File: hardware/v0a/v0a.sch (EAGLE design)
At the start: 117 parts, among them J1 2EDG-2P, J2 2EDG-2P, J3 2EDG-2P, J4 2EDG-2P, Q1 IRF7580, Q2 IRF7580, Q3 IRF7580, Q4 IRF7580, Q5 IRF7580, Q6 IRF7580, Q7 IRF7580, Q8 IRF7580, U1 TMC4671, U10 AD8418, U11 AD8418, U2 MIC39101, U3 MIC39101, U4 SI82397, U5 SI82397, U6 SI82397, U7 SI82397, U8 MIC4682, U9 CP2130

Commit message: temp
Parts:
- added C31: (no value), Passive Components > Capacitors > Multilayer Ceramic Capacitors MLCC:MLCC0603
- added C69, C70: 100p, Passive Components > Capacitors > Multilayer Ceramic Capacitors MLCC:MLCC0603
- added C71: 10n, Passive Components > Capacitors > Multilayer Ceramic Capacitors MLCC:MLCC0603
- added D8: BAT54S, Semiconductors > Discrete Semiconductors > Diodes & Rectifiers > Schottky Diodes & Rectifiers:BAT54S
- added R15, R16, R17, R18, R19, R20, R21, R22, R23, R24, R26, R32, R33, R34, R35: 10k, Passive Components > Resistors > Chip Resistors:RESISTOR0603
- added R25, R27: (no value), Passive Components > Resistors > Chip Resistors:RESISTOR0603
- added R28, R29, R30, R31: 2.2, Passive Components > Resistors > Chip Resistors:RESISTOR0603
- added R36, R37: 100, Passive Components > Resistors > Chip Resistors:RESISTOR0603
- added R38: 100k, Passive Components > Resistors > Chip Resistors:RESISTOR0603
- added R39: 1k5, Passive Components > Resistors > Chip Resistors:RESISTOR0603
- added U12: DSC1101, Eletromechanical > MEMS Oscillators:DSC1101
- R1, R2, R3, R4, R5, R6, R7, R8: value (none) -> 2.2
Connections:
- new net N$38: R15.P$2, U1-SENSO.PWM_IDLE_L@60
- new net N$39: R16.P$2, U1-SENSO.PWM_IDLE_H@59
- new net N$40: D4.A, R31.P$2
- new net N$41: U1-MISC.CLK@51, U12.OUT@4
- new net N$42: R27.P$2, U1-MISC.!RST!@50
- new net N$43: D3.A, R30.P$2
- new net N$44: R25.P$1, U12.EN@1
- new net N$48: D2.A, R29.P$2
- new net N$49: D1.A, R28.P$2
- new net N$50: C69.P$1, R36.P$1, U1-SENSO.ADC_I0_POS@16
- new net N$51: C70.P$1, R37.P$1, U1-SENSO.ADC_I1_POS@18
- new net N$52: R32.P$1, R33.P$2, U1-SENSO.ADC_I0_NEG@17
- new net N$53: R34.P$1, R35.P$2, U1-SENSO.ADC_I1_NEG@19
- new net N$54: C71.P$1, D8.3, R38.P$1, R39.P$2, U1-SENSO.ADC_VM@20
- net !CS: now also U1-IO.SPI_NSCS@6
- net 12V: now also R28.P$1, R29.P$1, R30.P$1, R31.P$1; no longer D1.A, D2.A, D3.A, D4.A
- net 3.3V: now also C31.P$1, R25.P$2, R27.P$1, U12.VDD@6
- net 5V: now also D8.1, R32.P$2, R34.P$2
- net ADC_I0_U_PF: now also R36.P$2
- net ADC_I1_V_PF: now also R37.P$2
- net DCBUS: now also R38.P$2
- net ENO: now also R26.P$1, U1-IO.ENO@32
- net GND: now also C31.P$2, C69.P$2, C70.P$2, C71.P$2, D8.2, R15.P$1, R16.P$1, R17.P$1, R18.P$1, R19.P$1, R20.P$1, R21.P$1, R22.P$1, R23.P$1, R24.P$1, R26.P$2, R33.P$1, R35.P$1, R39.P$1, U$10.GND@1, U1-MISC.TEST@54, U12.GND@3; no longer U$10.CASE
- net INT: now also U1-MISC.STATUS@12
- net MISO: now also U1-IO.SPI_MISO@9
- net MOSI: now also U1-IO.SPI_MOSI@8
- net N$11: no longer D2.C
- net N$30: now also U$10.D+; no longer U$10.VBUS
- net N$31: now also U$10.D-; no longer U$10.D+
- net N$32: now also U$10.VBUS; no longer U$10.D-
- net PWM_UX1_H: now also R17.P$2, U1-SENSO.PWM_UX1_H@39
- net PWM_UX1_L: now also R18.P$2, U1-SENSO.PWM_UX1_L@40
- net PWM_VX2_H: now also R19.P$2, U1-SENSO.PWM_VX2_H@41
- net PWM_VX2_L: now also R20.P$2, U1-SENSO.PWM_VX2_L@42
- net PWM_WY1_H: now also R21.P$2, U1-SENSO.PWM_WY1_H@46
- net PWM_WY1_L: now also R22.P$2, U1-SENSO.PWM_WY1_L@47
- net PWM_Y2_H: now also R23.P$2, U1-SENSO.PWM_Y2_H@48
- net PWM_Y2_L: now also R24.P$2, U1-SENSO.PWM_Y2_L@49
- net SCK: now also U1-IO.SPI_SCK@7
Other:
- moved on the sheet: D1, D2, D3, D4, U1-MISC

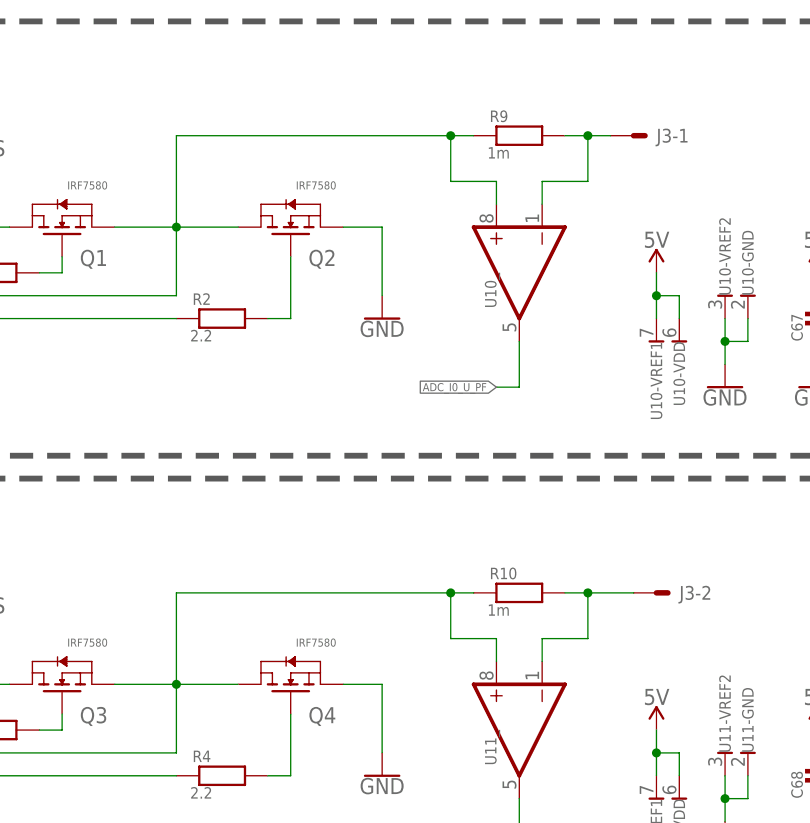
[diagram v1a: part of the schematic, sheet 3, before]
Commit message: changed current sense resistors to 700u
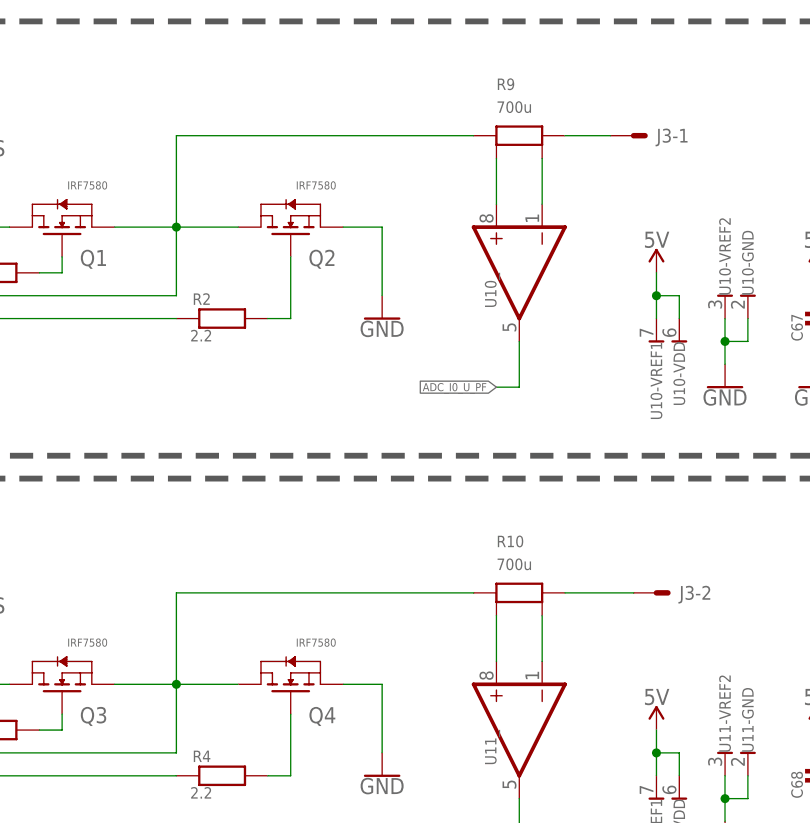
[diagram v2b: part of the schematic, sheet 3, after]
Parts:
- R10, R9: value 1m -> 700u; device Passive Components > Resistors > Current Sense:WSLF25121L000FEA -> Passive Components > Resistors > Current Sense:LRMAP3920
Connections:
- new net N$55: R10.SENSE-, U11_.IN-@1
- new net N$56: R10.SENSE+, U11_.IN+@8
- new net N$57: R9.SENSE-, U10_.IN-@1
- new net N$58: R9.SENSE+, U10_.IN+@8
- net N$10: no longer U11_.IN+@8
- net N$28: no longer U11_.IN-@1
- net N$29: no longer U10_.IN-@1
- net N$6: no longer U10_.IN+@8
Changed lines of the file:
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@@
 <part name="R8" library="Passive Components &gt; Resistors &gt; Chip Resistors" deviceset="RESISTOR" device="0603" value="2.2"/>
 <part name="J4" library="Connectors &gt; Other" deviceset="2EDG-2P" device=""/>
-<part name="R9" library="Passive Components &gt; Resistors &gt; Current Sense" deviceset="WSLF25121L000FEA" device="" value="1m"/>
 <part name="U10" library="Semiconductors &gt; Integrated Circuits - ICs &gt; Amplifier ICs &gt; Current Sense Amplifiers" deviceset="AD8418" device=""/>
 <part name="GND36" library="Utility &gt; Power Symbols" deviceset="GND" device=""/>
@@
 <part name="GND38" library="Utility &gt; Power Symbols" deviceset="GND" device=""/>
 <part name="C67" library="Passive Components &gt; Capacitors &gt; Multilayer Ceramic Capacitors MLCC" deviceset="MLCC" device="0603"/>
-<part name="R10" library="Passive Components &gt; Resistors &gt; Current Sense" deviceset="WSLF25121L000FEA" device="" value="1m"/>
 <part name="U11" library="Semiconductors &gt; Integrated Circuits - ICs &gt; Amplifier ICs &gt; Current Sense Amplifiers" deviceset="AD8418" device=""/>
 <part name="GND40" library="Utility &gt; Power Symbols" deviceset="GND" device=""/>
@@
 <part name="GND73" library="Utility &gt; Power Symbols" deviceset="GND" device=""/>
 <part name="GND74" library="Utility &gt; Power Symbols" deviceset="GND" device=""/>
+<part name="R9" library="Passive Components &gt; Resistors &gt; Current Sense" deviceset="LRMAP3920" device="" value="700u"/>
+<part name="R10" library="Passive Components &gt; Resistors &gt; Current Sense" deviceset="LRMAP3920" device="" value="700u"/>
 </parts>
 <sheets>
@@
 <attribute name="NAME" x="233.68" y="75.438" size="1.524" layer="95"/>
 </instance>
-<instance part="R9" gate="G$1" x="256.54" y="228.6" smashed="yes">
-<attribute name="NAME" x="253.238" y="230.124" size="1.27" layer="95"/>
-<attribute name="VALUE" x="252.984" y="226.06" size="1.27" layer="96"/>
-</instance>
 <instance part="U10" gate="_" x="256.54" y="208.28" smashed="yes" rot="MR270">
 <attribute name="NAME" x="254" y="213.36" size="1.27" layer="95" ratio="15" rot="MR270"/>
@@
 <attribute name="VALUE" x="292.1" y="205.74" size="1.27" layer="96" rot="R90"/>
 </instance>
-<instance part="R10" gate="G$1" x="256.54" y="177.8" smashed="yes">
-<attribute name="NAME" x="253.238" y="179.324" size="1.27" layer="95"/>
-<attribute name="VALUE" x="252.984" y="175.26" size="1.27" layer="96"/>
-</instance>
 <instance part="U11" gate="_" x="256.54" y="157.48" smashed="yes" rot="MR270">
 <attribute name="NAME" x="254" y="162.56" size="1.27" layer="95" ratio="15" rot="MR270"/>
@@
 <attribute name="NAME" x="144.018" y="82.804" size="1.27" layer="95"/>
 <attribute name="VALUE" x="143.764" y="78.74" size="1.27" layer="96"/>
+</instance>
+<instance part="R9" gate="G$1" x="256.54" y="228.6" smashed="yes">
+<attribute name="NAME" x="254" y="233.68" size="1.27" layer="95"/>
+<attribute name="VALUE" x="254" y="231.14" size="1.27" layer="96"/>
+</instance>
+<instance part="R10" gate="G$1" x="256.54" y="177.8" smashed="yes">
+<attribute name="NAME" x="254" y="182.88" size="1.27" layer="95"/>
+<attribute name="VALUE" x="254" y="180.34" size="1.27" layer="96"/>
 </instance>
 </instances>
@@
 <pinref part="Q1" gate="G$1" pin="S1"/>
 <pinref part="Q2" gate="G$1" pin="D1"/>
+<wire x1="218.44" y1="228.6" x2="251.46" y2="228.6" width="0.1524" layer="91"/>
 <pinref part="R9" gate="G$1" pin="P$1"/>
-<wire x1="251.46" y1="228.6" x2="248.92" y2="228.6" width="0.1524" layer="91"/>
-<wire x1="248.92" y1="228.6" x2="248.92" y2="223.52" width="0.1524" layer="91"/>
-<wire x1="248.92" y1="223.52" x2="254" y2="223.52" width="0.1524" layer="91"/>
-<pinref part="U10" gate="_" pin="IN+@8"/>
-<wire x1="254" y1="223.52" x2="254" y2="220.98" width="0.1524" layer="91"/>
-<wire x1="218.44" y1="228.6" x2="248.92" y2="228.6" width="0.1524" layer="91"/>
-<junction x="248.92" y="228.6"/>
 </segment>
 </net>
@@
 <pinref part="Q3" gate="G$1" pin="S1"/>
 <pinref part="Q4" gate="G$1" pin="D1"/>
+<wire x1="218.44" y1="177.8" x2="251.46" y2="177.8" width="0.1524" layer="91"/>
 <pinref part="R10" gate="G$1" pin="P$1"/>
-<wire x1="251.46" y1="177.8" x2="248.92" y2="177.8" width="0.1524" layer="91"/>
-<wire x1="248.92" y1="177.8" x2="248.92" y2="172.72" width="0.1524" layer="91"/>
-<wire x1="248.92" y1="172.72" x2="254" y2="172.72" width="0.1524" layer="91"/>
-<pinref part="U11" gate="_" pin="IN+@8"/>
-<wire x1="254" y1="172.72" x2="254" y2="170.18" width="0.1524" layer="91"/>
-<wire x1="218.44" y1="177.8" x2="248.92" y2="177.8" width="0.1524" layer="91"/>
-<junction x="248.92" y="177.8"/>
 </segment>
 </net>
@@
 <net name="N$29" class="0">
 <segment>
-<pinref part="U10" gate="_" pin="IN-@1"/>
-<wire x1="259.08" y1="220.98" x2="259.08" y2="223.52" width="0.1524" layer="91"/>
-<wire x1="259.08" y1="223.52" x2="264.16" y2="223.52" width="0.1524" layer="91"/>
-<wire x1="264.16" y1="223.52" x2="264.16" y2="228.6" width="0.1524" layer="91"/>
+<wire x1="261.62" y1="228.6" x2="266.7" y2="228.6" width="0.1524" layer="91"/>
+<pinref part="J3" gate="-1" pin="S"/>
 <pinref part="R9" gate="G$1" pin="P$2"/>
-<wire x1="264.16" y1="228.6" x2="261.62" y2="228.6" width="0.1524" layer="91"/>
-<wire x1="264.16" y1="228.6" x2="266.7" y2="228.6" width="0.1524" layer="91"/>
-<junction x="264.16" y="228.6"/>
-<pinref part="J3" gate="-1" pin="S"/>
 </segment>
 </net>
@@
 <net name="N$28" class="0">
 <segment>
-<wire x1="259.08" y1="172.72" x2="264.16" y2="172.72" width="0.1524" layer="91"/>
-<pinref part="U11" gate="_" pin="IN-@1"/>
-<wire x1="259.08" y1="170.18" x2="259.08" y2="172.72" width="0.1524" layer="91"/>
+<wire x1="269.24" y1="177.8" x2="261.62" y2="177.8" width="0.1524" layer="91"/>
+<pinref part="J3" gate="-2" pin="S"/>
 <pinref part="R10" gate="G$1" pin="P$2"/>
-<wire x1="269.24" y1="177.8" x2="264.16" y2="177.8" width="0.1524" layer="91"/>
-<pinref part="J3" gate="-2" pin="S"/>
-<wire x1="264.16" y1="177.8" x2="261.62" y2="177.8" width="0.1524" layer="91"/>
-<wire x1="264.16" y1="172.72" x2="264.16" y2="177.8" width="0.1524" layer="91"/>
-<junction x="264.16" y="177.8"/>
 </segment>
 </net>
@@
 </segment>
 </net>
+<net name="N$55" class="0">
+<segment>
+<pinref part="U11" gate="_" pin="IN-@1"/>
+<pinref part="R10" gate="G$1" pin="SENSE-"/>
+<wire x1="259.08" y1="170.18" x2="259.08" y2="175.26" width="0.1524" layer="91"/>
+</segment>
+</net>
+<net name="N$56" class="0">
+<segment>
+<pinref part="U11" gate="_" pin="IN+@8"/>
+<pinref part="R10" gate="G$1" pin="SENSE+"/>
+<wire x1="254" y1="170.18" x2="254" y2="175.26" width="0.1524" layer="91"/>
+</segment>
+</net>
+<net name="N$57" class="0">
+<segment>
+<pinref part="U10" gate="_" pin="IN-@1"/>
+<pinref part="R9" gate="G$1" pin="SENSE-"/>
+<wire x1="259.08" y1="226.06" x2="259.08" y2="220.98" width="0.1524" layer="91"/>
+</segment>
+</net>
+<net name="N$58" class="0">
+<segment>
+<pinref part="U10" gate="_" pin="IN+@8"/>
+<pinref part="R9" gate="G$1" pin="SENSE+"/>
+<wire x1="254" y1="226.06" x2="254" y2="220.98" width="0.1524" layer="91"/>
+</segment>
+</net>

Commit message: sch work
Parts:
- added C100, C101, C73, C74, C90, C91, C92, C93, C94, C95: 100n, Passive Components > Capacitors > Multilayer Ceramic Capacitors MLCC:MLCC0603
- added C102, C103: 100p, Passive Components > Capacitors > Multilayer Ceramic Capacitors MLCC:MLCC0603
- added C72: 1u, Passive Components > Capacitors > Tantalum Capacitors:CAPACITOR_TAN3216
- added C75: 4u7, Passive Components > Capacitors > Tantalum Capacitors:CAPACITOR_TAN3216
- added C76, C77, C78, C79, C80, C81, C82, C83, C84, C86, C87, C88, C89, C96, C97, C98, C99: (no value), Passive Components > Capacitors > Multilayer Ceramic Capacitors MLCC:MLCC0603
- added C85: 1u, Passive Components > Capacitors > Multilayer Ceramic Capacitors MLCC:MLCC0603
- added D10, D11: (no value), Opto-electronics > LED Emitters:LED0603
- added D9: SP0503BAHT, Circuit Protection > ESD Suppressors \ TVS Diodes:SP0503BAHT
- added J5, J6, J7, J8: SH-5, Connectors > JST > SH:SH-5
- added J9: SH-2, Connectors > JST > SH:SH-2
- added R40: 24k, Passive Components > Resistors > Chip Resistors:RESISTOR0603
- added R41: 47k, Passive Components > Resistors > Chip Resistors:RESISTOR0603
- added R42, R43, R44, R45, R46, R48, R49, R50, R51, R52, R53, R54, R57, R60, R70, R71, R72: (no value), Passive Components > Resistors > Chip Resistors:RESISTOR0603
- added R47: (no value), Passive Components > Thermistors > NTC:NTC0603
- added R61, R62, R63, R64, R65, R66, R67, R68, R69, R73, R74, R75: 100k, Passive Components > Resistors > Chip Resistors:RESISTOR0603
- added R76, R77: 100, Passive Components > Resistors > Chip Resistors:RESISTOR0603
- added U$12: USB-SHIELD, Connectors > USB:USB-SHIELD
- added U$13: CP2102N, Semiconductors > Integrated Circuits - ICs > Interface ICs > USB Interface IC:CP2102N
- added U$15, U$16, U$17, U$18: SRV05-4, Circuit Protection > ESD Suppressors \ TVS Diodes:SRV05-4
- added U13, U14, U15, U16: 74LVC3G17, Semiconductors > Integrated Circuits - ICs > Logic ICs > Logic Gates:74LVC3G17
- R38: value 100k -> 140k
- R39: value 1k5 -> 10k
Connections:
- new net ADC_T_MOSFETS: C77.P$2, R45.P$2, R47.P$1, R76.P$2
- new net ADC_T_MOTOR: C76.P$2, J9-2.S, R46.P$2, R77.P$1
- new net BRAKE: U1-SENSO.BRAKE@31
- new net CP2102_RX: U$13.RXD@20, U1-IO.TXD_SYNCO@11
- new net CP2102_TX: U$13.TXD@21, U1-IO.RXD_SYNCI@10
- new net DBG_SPI_MISO: U1-IO.GPIO6@4
- new net DBG_SPI_MOSI: U1-IO.GPIO5@1
- new net DBG_SPI_NSCS: U1-IO.GPIO3@75
- new net DBG_SPI_SCK: U1-IO.GPIO4@76
- new net DBG_SPI_TRG: U1-IO.GPIO7@5
- new net DIR: U1-IO.DIR@56
- new net ENC2_A: U1-SENSO.ENC2_A@64, U14.1.Y
- new net ENC2_B: U1-SENSO.ENC2_B@65, U14.2.Y
- new net ENC2_N: U1-SENSO.ENC2_N@66, U14.3.Y
- new net ENC_A: U1-SENSO.ENC_A@35, U13.1.Y
- new net ENC_B: U1-SENSO.ENC_B@34, U13.2.Y
- new net ENC_N: U1-SENSO.ENC_N@33, U13.3.Y
- new net GPIO0: U1-IO.GPIO0@70
- new net GPIO1: U1-IO.GPIO1@71
- new net GPIO2: U1-IO.GPIO2@74
- new net HALL_UX: U1-SENSO.HALL_UX@38, U15.3.Y
- new net HALL_V: U1-SENSO.HALL_V@37, U15.2.Y
- new net HALL_WY: U1-SENSO.HALL_WY@36, U15.1.Y
- new net N$59: D9.4, R40.P$1, U$12.VBUS
- new net N$60: D9.3, U$12.D+, U$13.D+@3
- new net N$61: D9.2, U$12.D-, U$13.D-@4
- new net N$62: R40.P$2, R41.P$1, U$13.VBUS@8
- new net N$63: D11.CA, U$13.GPIO0-TXT@14
- new net N$64: D10.CA, U$13.GPIO1-RXT@13
- new net N$65: D11.AN, R42.P$1
- new net N$66: D10.AN, R43.P$1
- new net N$67: C80.P$1, R50.P$2, R69.P$2, U$15.3, U13.3.A
- new net N$68: R44.P$1, U$13.RSTB@9
- new net N$69: C79.P$1, R49.P$2, R68.P$2, U$15.2, U13.2.A
- new net N$70: C84.P$1, R53.P$2, R66.P$2, U$16.3, U14.3.A
- new net N$71: J5-2.S, R48.P$1
- new net N$72: J5-3.S, R49.P$1
- new net N$73: J5-4.S, R50.P$1
- new net N$74: C78.P$1, R48.P$2, R67.P$2, U$15.1, U13.1.A
- new net N$75: C83.P$1, R52.P$2, R65.P$2, U$16.2, U14.2.A
- new net N$76: J6-2.S, R51.P$1
- new net N$77: J6-3.S, R52.P$1
- new net N$78: J6-4.S, R53.P$1
- new net N$79: C82.P$1, R51.P$2, R64.P$2, U$16.1, U14.1.A
- new net N$80: C88.P$1, R60.P$2, R63.P$2, U$17.3, U15.3.A
- new net N$81: C87.P$1, R57.P$2, R62.P$2, U$17.2, U15.2.A
- new net N$82: J7-2.S, R54.P$1
- new net N$83: J7-3.S, R57.P$1
- new net N$84: J7-4.S, R60.P$1
- new net N$85: C86.P$1, R54.P$2, R61.P$2, U$17.1, U15.1.A
- new net N$86: C98.P$1, R72.P$2, R75.P$2, U$18.3, U16.3.A
- new net N$87: C97.P$1, R71.P$2, R74.P$2, U$18.2, U16.2.A
- new net N$88: J8-2.S, R70.P$1
- new net N$89: J8-3.S, R71.P$1
- new net N$90: J8-4.S, R72.P$1
- new net N$91: C96.P$1, R70.P$2, R73.P$2, U$18.1, U16.1.A
- new net N$92: C102.P$1, R76.P$1, U1-IO.AGPI_A@21
- new net N$93: C103.P$1, R77.P$2, U1-IO.AGPI_B@22
- new net PWM_IN: U1-IO.PWM_IN@58
- new net REF_H: U1-SENSO.REF_H@68, U16.2.Y
- new net REF_L: U1-SENSO.REF_L@67, U16.3.Y
- new net REF_R: U1-SENSO.REF_R@69, U16.1.Y
- new net STEP: U1-IO.STP@57
- net 3.3V: now also C101.P$1, C72.AN, C73.P$1, C74.P$1, C75.AN, C92.P$1, C94.P$1, C95.P$1, R42.P$2, R43.P$2, R44.P$2, U13.PW.VCC, U14.PW.VCC, U15.PW.VCC, U16.PW.VCC
- net 5V: now also C100.P$1, C81.P$1, C85.P$1, C89.P$1, C90.P$1, C91.P$1, C93.P$1, C99.P$1, D8.2, J5-1.S, J6-1.S, J7-1.S, J8-1.S, J9-1.S, R47.P$2, R61.P$1, R62.P$1, R63.P$1, R64.P$1, R65.P$1, R66.P$1, R67.P$1, R68.P$1, R69.P$1, R73.P$1, R74.P$1, R75.P$1, U$15.VCC, U$16.VCC, U$17.VCC, U$18.VCC; no longer D8.1
- net GND: now also C100.P$2, C101.P$2, C102.P$2, C103.P$2, C72.CA, C73.P$2, C74.P$2, C75.CA, C76.P$1, C77.P$1, C78.P$2, C79.P$2, C80.P$2, C81.P$2, C82.P$2, C83.P$2, C84.P$2, C85.P$2, C86.P$2, C87.P$2, C88.P$2, C89.P$2, C90.P$2, C91.P$2, C92.P$2, C93.P$2, C94.P$2, C95.P$2, C96.P$2, C97.P$2, C98.P$2, C99.P$2, D8.1, D9.1, J5-5.S, J5-CASE.S, J6-5.S, J6-CASE.S, J7-5.S, J7-CASE.S, J8-5.S, J8-CASE.S, J9-CASE.S, R41.P$2, R45.P$1, R46.P$1, U$10.CASE, U$12.CASE, U$12.GND, U$15.GND, U$16.GND, U$17.GND, U$18.GND, U13.PW.GND, U14.PW.GND, U15.PW.GND, U16.PW.GND; no longer D8.2, U$10.GND@1
- net N$30: now also U$10.VBUS; no longer U$10.D+
- net N$31: now also U$10.D+; no longer U$10.D-
- net N$32: now also U$10.D-; no longer U$10.VBUS
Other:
- note added: "4/60V/V"
- note added: "Feedback"
